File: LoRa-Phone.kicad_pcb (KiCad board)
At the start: 4 copper layers, 60 x 102.5 mm, 155 parts, among them IC1 SKY13373-460LF, IC2 AD8318ACPZ-REEL7, IC3 AD8318ACPZ-REEL7, IC4 TPS2121RUXT, IC5 MAX17048G+T10, IC6 MAX17048G+T10, IC7 TCA9543ADR, J1 Interface, J2 Connector, J3 Connector, J4 BUTTON, J4 JST_MAIN, J6 ROTARY_ENCODER, M1 Motor_DC, U1 ESP32-S3-WROOM-2, U10 DRV2605LDGS, U11 LC76G, U13 SA818S, U2 TCD-10-23BDX+, U21 WM8960, U23 E22-900M30S, U24 E22-170M30S, U3 MCP23017x-x-ML, U4 BMP390, U5 IS31FL3218-QF, U6 LSM6DSOXTR, U7 BQ24075RGT, U8 MCP23017x-x-ML, U9 BQ24075RGT

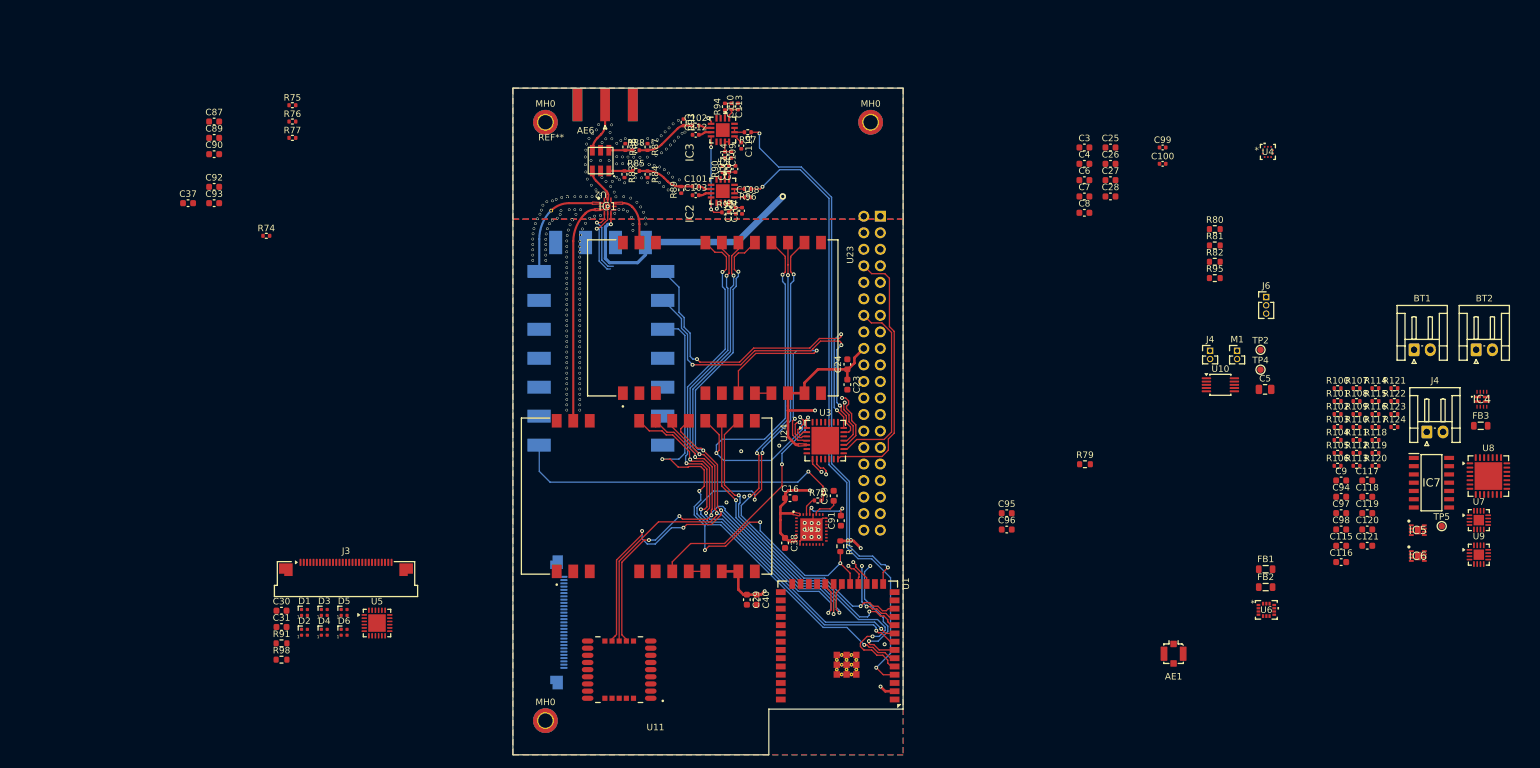
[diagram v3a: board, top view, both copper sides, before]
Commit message: Routed secondary PCB with Power and charging managment, and routed FPC Connector
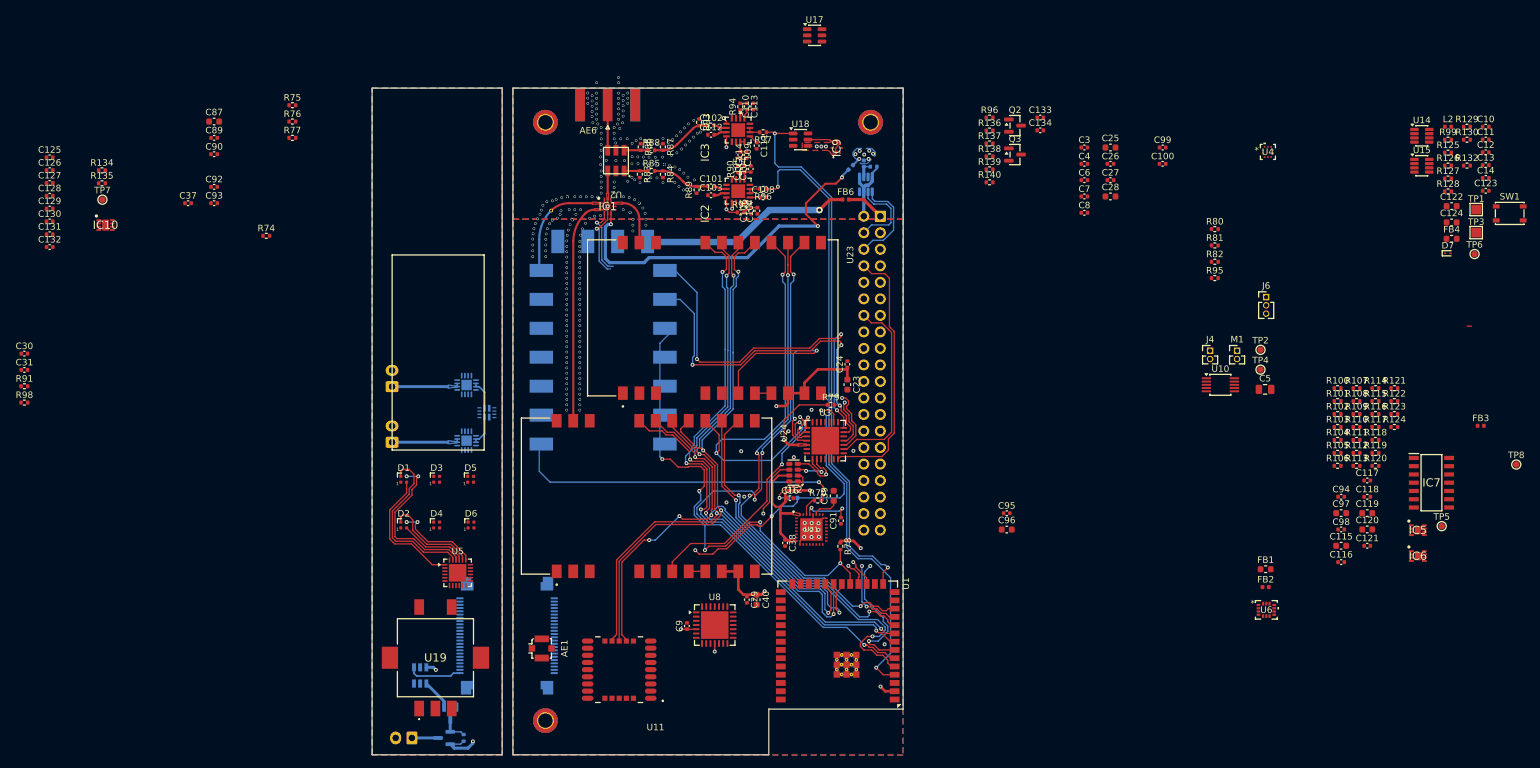
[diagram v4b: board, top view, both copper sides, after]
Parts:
- removed J2: Connector, Connector_FFC-FPC:Amphenol_F32R-1A7x1-11029_1x29-1MP_P0.5mm_Horizontal
- added C10: 100pF, Capacitor_SMD:C_0402_1005Metric, F.Cu at (266.2, 57.2)
- added C11: NC, Capacitor_SMD:C_0402_1005Metric, F.Cu at (266.2, 59.2)
- added C12: NC, Capacitor_SMD:C_0402_1005Metric, F.Cu at (266.2, 61.1)
- added C122: 100nF, Capacitor_SMD:C_0603_1608Metric, F.Cu at (260.9, 69.4)
- added C123: 100nF, Capacitor_SMD:C_0402_1005Metric, F.Cu at (266.2, 67.0)
- added C124: 100nF, Capacitor_SMD:C_0603_1608Metric, F.Cu at (260.9, 71.9)
- added C125: 100nF, Capacitor_SMD:C_0402_1005Metric, F.Cu at (45.4, 61.9)
- added C126: 2.2uF, Capacitor_SMD:C_0402_1005Metric, F.Cu at (45.4, 63.9)
- added C127: 2.2uF, Capacitor_SMD:C_0402_1005Metric, F.Cu at (45.4, 65.8)
- added C128: 100nF, Capacitor_SMD:C_0402_1005Metric, F.Cu at (45.4, 67.8)
- added C129: 2.2uF, Capacitor_SMD:C_0402_1005Metric, F.Cu at (45.4, 69.8)
- added C13: 100nF, Capacitor_SMD:C_0402_1005Metric, F.Cu at (266.2, 63.1)
- added C130: 100nF, Capacitor_SMD:C_0402_1005Metric, F.Cu at (45.4, 71.7)
- added C131: 100nF, Capacitor_SMD:C_0402_1005Metric, F.Cu at (45.4, 73.7)
- added C132: 100nF, Capacitor_SMD:C_0402_1005Metric, F.Cu at (45.4, 75.7)
- added C133: 100nF, Capacitor_SMD:C_0402_1005Metric, F.Cu at (197.7, 55.8)
- added C134: 100nF, Capacitor_SMD:C_0402_1005Metric, F.Cu at (197.7, 57.7)
- added C14: 100pF, Capacitor_SMD:C_0402_1005Metric, F.Cu at (266.2, 65.1)
- added D7: D_TVS, Diode_SMD:D_SOD-923, F.Cu at (260.3, 76.6)
- added D8: D, Diode_SMD:D_SOD-523, B.Cu at (159.6, 114.3)
- added FB4: 600R @100MHz 1.5A, Inductor_SMD:L_0603_1608Metric, F.Cu at (260.9, 74.4)
- added FB5: 600R @100MHz 500mA, Inductor_SMD:L_0402_1005Metric, B.Cu at (168.5, 63.4)
- added FB6: 600R @100MHz 500mA, Inductor_SMD:L_0402_1005Metric, F.Cu at (167.8, 68.4)
- added FB7: 600R @100MHz 4A, Inductor_SMD:L_0402_1005Metric, B.Cu at (170.6, 62.8)
- added IC10: TPS22965NTDSGRQ1, PTCR:SON50P200X200X80-9N, F.Cu at (54.0, 72.3)
- added IC8: MAX16150AUT+T, PTCR:SOT95P280X145-6N, B.Cu at (102.3, 141.6)
- added IC9: SN74LVC1G74RSE2, PTCR:SN74LVC1G74RSE2, F.Cu at (166.4, 60.4)
- added J5: Board_2, Connector_FFC-FPC:Amphenol_F32Q-1A7x1-11024_1x24-1MP_P0.5mm_Horizontal, B.Cu at (111.4, 135.4)
- added L2: 68nH, Inductor_SMD:L_0402_1005Metric, F.Cu at (260.4, 57.2)
- added Q1: AO3400A, Package_TO_SOT_SMD:SOT-23, B.Cu at (107.0, 147.4)
- added Q2: AO3400A, Package_TO_SOT_SMD:SOT-23, F.Cu at (193.8, 57.0)
- added Q3: AO3400A, Package_TO_SOT_SMD:SOT-23, F.Cu at (193.8, 61.5)
- added Q4: AO3401A, Package_TO_SOT_SMD:SOT-23, B.Cu at (106.0, 151.2)
- added R125: 0R, Resistor_SMD:R_0402_1005Metric, F.Cu at (260.4, 61.2)
- added R126: 10R, Resistor_SMD:R_0402_1005Metric, F.Cu at (260.4, 63.2)
- added R127: 0.02R, Resistor_SMD:R_0402_1005Metric, F.Cu at (260.4, 65.2)
- added R128: 51.1K, Resistor_SMD:R_0402_1005Metric, F.Cu at (260.4, 67.1)
- added R129: 10K, Resistor_SMD:R_0402_1005Metric, F.Cu at (263.3, 57.2)
- added R130: 0.05R, Resistor_SMD:R_0402_1005Metric, F.Cu at (263.3, 59.2)
- added R131: 0.01R, Resistor_SMD:R_0402_1005Metric, B.Cu at (172.1, 63.3)
- added R132: 10K, Resistor_SMD:R_0402_1005Metric, F.Cu at (263.3, 63.2)
- added R133: 100K, Resistor_SMD:R_0402_1005Metric, B.Cu at (109.0, 151.2)
- added R134: 5K, Resistor_SMD:R_0402_1005Metric, F.Cu at (53.4, 63.9)
- added R135: 1K, Resistor_SMD:R_0402_1005Metric, F.Cu at (53.4, 65.9)
- added R136: 10K 0.1%, Resistor_SMD:R_0402_1005Metric, F.Cu at (189.9, 57.8)
- added R137: 5.6K 0.1%, Resistor_SMD:R_0402_1005Metric, F.Cu at (189.9, 59.8)
- added R138: 10K 0.1%, Resistor_SMD:R_0402_1005Metric, F.Cu at (189.9, 61.8)
- added R139: 10K, Resistor_SMD:R_0402_1005Metric, F.Cu at (189.9, 63.7)
- added R140: 10K, Resistor_SMD:R_0402_1005Metric, F.Cu at (189.9, 65.7)
- added R96: 10K, Resistor_SMD:R_0402_1005Metric, F.Cu at (189.9, 55.8)
- added R99: 10K, Resistor_SMD:R_0402_1005Metric, F.Cu at (260.4, 59.2)
- added SW1: POWER, Button_Switch_SMD:SW_SPST_PTS810, F.Cu at (269.9, 70.5)
- added TP1: TXD_LC76G, TestPoint:TestPoint_Pad_1.5x1.5mm, F.Cu at (264.7, 69.9)
- added TP3: RXD_LC76G, TestPoint:TestPoint_Pad_1.5x1.5mm, F.Cu at (264.7, 73.5)
- added TP6: +3V3_RF, TestPoint:TestPoint_Pad_D1.0mm, F.Cu at (264.5, 76.8)
- added TP7: +3V3_RF, TestPoint:TestPoint_Pad_D1.0mm, F.Cu at (53.5, 68.4)
- added TP8: +5V_RF, TestPoint:TestPoint_Pad_D1.0mm, F.Cu at (270.9, 109.1)
- added U12: RV-3028-C7, Package_SON:MicroCrystal_C7_SON-8_1.5x3.2mm_P0.9mm, F.Cu at (159.7, 110.4)
- added U14: INA219BxDCN, Package_TO_SOT_SMD:SOT-23-8, F.Cu at (256.3, 58.6)
- added U15: INA219BxDCN, Package_TO_SOT_SMD:SOT-23-8, F.Cu at (256.3, 63.2)
- added U16: INA219BxDCN, Package_TO_SOT_SMD:SOT-23-8, B.Cu at (170.9, 66.0)
- added U17: MCP4725xxx-xCH, Package_TO_SOT_SMD:SOT-23-6, F.Cu at (163.0, 43.1)
- added U18: TLV3501AIDBV, Package_TO_SOT_SMD:SOT-23-6, F.Cu at (160.8, 59.2)
- added U19: RIC11-31S10K2-GSMT, PTCR:RIC1131S10K2GSMT, F.Cu at (104.7, 138.8)
- BT1, BT2, IC4, J4, U7, U9: moved to B.Cu
- C116, C117, C118, C121, C16, C24, C26, C27, C29, C3, C30, C31, C37, C38, C4, C6, C7, C8, C89, C9, C90, C91, C92, C93, C94, C95, C98: footprint Capacitor_SMD:C_0603_1608Metric -> Capacitor_SMD:C_0402_1005Metric
- FB1: value FerriteBead -> 600R @100MHz 2A; footprint Inductor_SMD:L_0805_2012Metric -> Inductor_SMD:L_0603_1608Metric
- FB2, FB3: value FerriteBead -> 600R @100MHz 500mA; footprint Inductor_SMD:L_0805_2012Metric -> Inductor_SMD:L_0402_1005Metric
- J3: value Connector -> Board_1; footprint Connector_FFC-FPC:Amphenol_F32R-1A7x1-11029_1x29-1MP_P0.5mm_Horizontal -> Connector_FFC-FPC:Amphenol_F32Q-1A7x1-11024_1x24-1MP_P0.5mm_Horizontal; moved to B.Cu
- R100: value 13.7K -> 16K
- R101: value 23.7K -> 16K
- R78, R79, R80, R81, R82, R91, R95, R98: footprint Resistor_SMD:R_0603_1608Metric -> Resistor_SMD:R_0402_1005Metric
- R97: value 1K -> 5.6K 0.1%
- TP5: value +3V3_RF -> +5V_RF
- moved BT2 167.3 mm to (98.0, 105.7), turned to 90 degrees
- moved J4 163.0 mm to (101.1, 151.2), turned to 180 degrees
- moved BT1 157.2 mm to (98.0, 97.2), turned to 90 degrees
- moved U7 157.0 mm to (109.5, 96.9)
- moved U9 156.6 mm to (109.5, 105.5)
- moved IC4 153.0 mm to (112.6, 101.2), turned to 90 degrees
- moved U8 121.1 mm to (147.6, 133.8)
- moved C9 103.1 mm to (143.3, 133.9), turned to 90 degrees
- moved AE1 97.1 mm to (121.0, 137.4), turned to 90 degrees
- moved C30 55.9 mm to (41.5, 92.1)
- moved R91 55.9 mm to (41.5, 97.1)
- moved R98 55.9 mm to (41.5, 99.6)
- moved C31 55.9 mm to (41.5, 94.6)
- moved R79 40.1 mm to (165.5, 100.0)
- moved J3 30.3 mm to (120.0, 135.4), turned to 90 degrees
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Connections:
- AE1 pad 1: RF_IN -> Net-(AE1-A)
- C104 pad 1: +3V3_RF -> +5V_RF
- C105 pad 1: +3V3_RF -> +5V_RF
- C106 pad 2: +3V3_RF -> +5V_RF
- C107 pad 2: +3V3_RF -> +5V_RF
- C109 pad 1: +3V3_RF -> +5V_RF
- C110 pad 1: +3V3_RF -> +5V_RF
- C113 pad 2: +3V3_RF -> +5V_RF
- C114 pad 2: +3V3_RF -> +5V_RF
- C23 pad 1: +3V3 -> +3V3_RADIO
- C24 pad 1: +3V3 -> +3V3_RADIO
- C29 pad 1: +3V3 -> +3V3_RADIO
- C37 pad 1: Net-(U21-DBVDD) -> +3V3
- C40 pad 1: +3V3 -> +3V3_RADIO
- C95 pad 1: +3V3 -> +5V_RADIO
- C96 pad 1: +3V3 -> +5V_RADIO
- D1 pad 1: GND -> +3V3
- D2 pad 1: GND -> +3V3
- D3 pad 1: GND -> +3V3
- D4 pad 1: GND -> +3V3
- D5 pad 1: GND -> +3V3
- D6 pad 1: GND -> +3V3
- FB2 pad 1: +3V3_GNSS -> +3V3_GNSS_IN
- FB3 pad 1: +3V3_RF -> +5V_RF
- FB3 pad 2: +3V3 -> +5V
- IC2 pad 3: +3V3_RF -> +5V_RF
- IC2 pad 4: +3V3_RF -> +5V_RF
- IC2 pad 9: +3V3_RF -> +5V_RF
- IC3 pad 16: AD8318_EN -> Net-(IC3-ENBL)
- IC3 pad 3: +3V3_RF -> +5V_RF
- IC3 pad 4: +3V3_RF -> +5V_RF
- IC3 pad 9: +3V3_RF -> +5V_RF
- IC5 pad 7: SD0 -> SC0
- IC5 pad 8: SC0 -> SD0
- IC6 pad 7: SD1 -> SC1
- IC6 pad 8: SC1 -> SD1
- J1 pad 18: +3V3 -> +3V3_RAW
- J1 pad 2: +3V3 -> +3V3_RAW
- J3 pad 1: +3V3 -> POWER_BTN
- J3 pad 10: D5B -> SHUTDOWN_1
- J3 pad 11: D6R -> BAT_VAL_1
- J3 pad 12: D6G -> BATS_RESET_1
- J3 pad 13: D6B -> BATS_INT_1
- J3 pad 14: GND -> +3V3
- J3 pad 15: GND -> BAT1_PGOOD_1
- J3 pad 16: ROT_ENC2_B -> BAT1_CHG_1
- J3 pad 17: ROT_ENC1_B -> BAT2_PGOOD_1
- J3 pad 18: BUTTON0_B -> BAT2_CHG_1
- J3 pad 19: D1R -> SDA
- J3 pad 2: +3V3 -> GND
- J3 pad 20: D1G -> JOYSTICK_X
- J3 pad 21: D1B -> JOYSTICK_Y
- J3 pad 22: D2R -> BUTTON1
- J3 pad 23: D2G -> +3V3
- J3 pad 24: D2B -> +3V3
- J3 pad 3: BUTTON1_B -> GND
- J3 pad 4: JOYSTICK_Y_B -> GND
- J3 pad 5: JOYSTICK_X_B -> BUTTON0
- J3 pad 6: SDA -> ROT_ENC1
- J3 pad 7: SCL -> ROT_ENC2
- J3 pad 8: D5R -> SCL
- J3 pad 9: D5G -> BAT_SEL_1
- J4 pad 1: BAT_OUT -> Net-(J4-Pin_1)
- R92 pad 1: AD8318_EN -> Net-(IC3-ENBL)
- R92 pad 2: +3V3_RF -> +5V_RF
- TP4 pad 1: +3V3_GNSS -> +3V3_GNSS_IN
- TP5 pad 1: +3V3_RF -> +5V_RF
- U1 pad 35: unconnected-(U1-MTMS/IO42-Pad35) -> CS_GNSS
- U11 pad 11: RF_IN -> Net-(U11-RF_IN)
- U11 pad 14: Net-(U11-VDD_RF) -> VDD_RF
- U11 pad 16: SDA -> unconnected-(U11-I2C_SDA-Pad16)
- U11 pad 17: SCL -> unconnected-(U11-I2C_SCL-Pad17)
- U11 pad 2: TXD1 -> Net-(U11-TXD)
- U11 pad 24: unconnected-(U11-D_SEL-Pad24) -> Net-(U11-D_SEL)
- U11 pad 3: RXD1 -> Net-(U11-RXD)
- U13 pad 8: +3V3 -> +5V_RADIO
- U21 pad 10: Net-(U21-DBVDD) -> +3V3
- U23 pad 10: +3V3 -> +3V3_RADIO
- U23 pad 16: MOSI -> MISO
- U23 pad 17: MISO -> MOSI
- U23 pad 9: +3V3 -> +3V3_RADIO
- U24 pad 10: +3V3 -> +3V3_RADIO
- U24 pad 16: MOSI -> MISO
- U24 pad 17: MISO -> MOSI
- U24 pad 9: +3V3 -> +3V3_RADIO
- U3 pad 16: INTA_MCP -> INTA_MCP_1
- U3 pad 22: RFS_V2 -> INT_RTC
- U3 pad 23: RFS_V1 -> POWER_BTN
- U3 pad 26: unconnected-(U3-GPB1-Pad26) -> RFS_V2
- U3 pad 27: unconnected-(U3-GPB2-Pad27) -> RFS_V1
- U5 pad 1: D1R_A -> D1R
- U5 pad 10: D5B_A -> D5B
- U5 pad 11: D5G_A -> D5G
- U5 pad 12: D5R_A -> D5R
- U5 pad 13: D4B_A -> D4B
- U5 pad 14: D4G_A -> D4G
- U5 pad 15: D4R_A -> D4R
- U5 pad 16: D3B_A -> D3B
- U5 pad 17: D3G_A -> D3G
- U5 pad 18: D3R_A -> D3R
- U5 pad 19: D2B_A -> D2B
- U5 pad 20: D2G_A -> D2G
- U5 pad 21: D2R_A -> D2R
- U5 pad 22: D1B_A -> D1B
- U5 pad 23: D1G_A -> D1G
- U5 pad 7: D6B_A -> D6B
- U5 pad 8: D6G_A -> D6G
- U5 pad 9: D6R_A -> D6R
- U8 pad 1: unconnected-(U8-GPB4-Pad1) -> SHDN_COMP
- U8 pad 16: INTA_MCP -> INTA_MCP_2
- U8 pad 17: BAT1_PGOOD -> BAT1_PGOOD_1
- U8 pad 18: BAT1_CHG -> BAT1_CHG_1
- U8 pad 19: BAT2_PGOOD -> BAT2_PGOOD_1
- U8 pad 2: unconnected-(U8-GPB5-Pad2) -> BAT_SEL_1
- U8 pad 20: BAT2_CHG -> BAT2_CHG_1
- U8 pad 21: BATS_INT -> BATS_INT_1
- U8 pad 22: BATS_RESET -> BATS_RESET_1
- U8 pad 23: unconnected-(U8-GPA6-Pad23) -> BAT_VAL_1
- U8 pad 25: unconnected-(U8-GPB0-Pad25) -> G_RESET
- U8 pad 26: unconnected-(U8-GPB1-Pad26) -> SHUTDOWN_1
- U8 pad 27: unconnected-(U8-GPB2-Pad27) -> RF_FAULT
- U8 pad 28: unconnected-(U8-GPB3-Pad28) -> RF_FAULT_RESET
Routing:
- net +3V3: track 101.1 -> 46.3 mm, vias 7 -> 16
- net POWER_BTN: track 0.00 -> 45.2 mm, vias 0 -> 3
- net +3V3_RF: track 12.1 -> 56.0 mm, vias 0 -> 3
- net +5V_RADIO: track 0.00 -> 33.0 mm, vias 0 -> 1
- net INTA_MCP_1: track 0.00 -> 29.1 mm
- net INTA_MCP: track 29.1 -> 0.00 mm
- net +3V3_RADIO: track 0.00 -> 26.6 mm, vias 0 -> 2
- net D1G: track 0.00 -> 25.4 mm
- net D1B: track 0.00 -> 23.7 mm, vias 0 -> 2
- net D1R: track 0.00 -> 19.9 mm
- net SCL: track 2.62 -> 20.6 mm, vias 1 -> 2
- net SDA: track 3.22 -> 20.7 mm
- net BAT_OUT: track 0.00 -> 17.4 mm, vias 0 -> 3
- net D2G: track 0.00 -> 14.6 mm
- net D2B: track 0.00 -> 13.0 mm, vias 0 -> 2
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- added copper zone on B.Cu, net +3V3
- added copper zone on B.Cu, net BAT1
- added copper zone on B.Cu, net BAT2
- added copper zone on In2.Cu, net BAT_OUT
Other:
- board size 60 x 102.5 mm -> 81.6 x 102.5 mm
